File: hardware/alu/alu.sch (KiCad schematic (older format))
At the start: 68 parts, among them J1 Conn_ALU, J2 Conn_Power, U1 74LVC1G02, U10 74AUC2G04, U11 74HC4017, U12 74LVC1G157, U13 74HC595, U14 74HC86, U15 74LVC1G32, U16 74LVC1G08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

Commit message: Unified footprints
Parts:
- U21, U22, U23, U24, U5: footprint Package_TO_SOT_SMD:SOT-23-5 -> Package_TO_SOT_SMD:SOT-23-5_HandSoldering
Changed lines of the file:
@@
 F 0 "U5" H 14400 6617 50  0000 C CNN
 F 1 "MIC5504-3.3YM5" H 14400 6526 50  0000 C CNN
-F 2 "Package_TO_SOT_SMD:SOT-23-5" H 14400 5850 50  0001 C CNN
+F 2 "Package_TO_SOT_SMD:SOT-23-5_HandSoldering" H 14400 5850 50  0001 C CNN
 F 3 "http://ww1.microchip.com/downloads/en/DeviceDoc/MIC550X.pdf" H 14150 6500 50  0001 C CNN
 	1    14400 6250
@@
 F 0 "U21" H 19300 4017 50  0000 C CNN
 F 1 "74LVC1G04" H 19300 3926 50  0000 C CNN
-F 2 "Package_TO_SOT_SMD:SOT-23-5" H 19300 3750 50  0001 C CNN
+F 2 "Package_TO_SOT_SMD:SOT-23-5_HandSoldering" H 19300 3750 50  0001 C CNN
 F 3 "" H 19300 3750 50  0001 C CNN
 	1    19300 3750
@@
 F 0 "U21" H 19800 11150 50  0000 L CNN
 F 1 "74LVC1G04" V 19600 11550 50  0000 C CNN
-F 2 "Package_TO_SOT_SMD:SOT-23-5" H 19750 11550 50  0001 C CNN
+F 2 "Package_TO_SOT_SMD:SOT-23-5_HandSoldering" H 19750 11550 50  0001 C CNN
 F 3 "" H 19750 11550 50  0001 C CNN
 	2    19750 11550
@@
 F 0 "U23" H 19100 6217 50  0000 C CNN
 F 1 "74LVC1G04" H 19100 6126 50  0000 C CNN
-F 2 "Package_TO_SOT_SMD:SOT-23-5" H 19100 5950 50  0001 C CNN
+F 2 "Package_TO_SOT_SMD:SOT-23-5_HandSoldering" H 19100 5950 50  0001 C CNN
 F 3 "" H 19100 5950 50  0001 C CNN
 	1    19100 5950
@@
 F 0 "U22" H 21000 4017 50  0000 C CNN
 F 1 "74LVC1G04" H 21000 3926 50  0000 C CNN
-F 2 "Package_TO_SOT_SMD:SOT-23-5" H 21000 3750 50  0001 C CNN
+F 2 "Package_TO_SOT_SMD:SOT-23-5_HandSoldering" H 21000 3750 50  0001 C CNN
 F 3 "" H 21000 3750 50  0001 C CNN
 	1    21000 3750
@@
 F 0 "U24" H 20900 6267 50  0000 C CNN
 F 1 "74LVC1G04" H 20900 6176 50  0000 C CNN
-F 2 "Package_TO_SOT_SMD:SOT-23-5" H 20900 6000 50  0001 C CNN
+F 2 "Package_TO_SOT_SMD:SOT-23-5_HandSoldering" H 20900 6000 50  0001 C CNN
 F 3 "" H 20900 6000 50  0001 C CNN
 	1    20900 6000
@@
 F 0 "U22" H 20200 11150 50  0000 L CNN
 F 1 "74LVC1G04" V 20000 11550 50  0000 C CNN
-F 2 "Package_TO_SOT_SMD:SOT-23-5" H 20150 11550 50  0001 C CNN
+F 2 "Package_TO_SOT_SMD:SOT-23-5_HandSoldering" H 20150 11550 50  0001 C CNN
 F 3 "" H 20150 11550 50  0001 C CNN
 	2    20150 11550
@@
 F 0 "U23" H 20600 11150 50  0000 L CNN
 F 1 "74LVC1G04" V 20400 11550 50  0000 C CNN
-F 2 "Package_TO_SOT_SMD:SOT-23-5" H 20550 11550 50  0001 C CNN
+F 2 "Package_TO_SOT_SMD:SOT-23-5_HandSoldering" H 20550 11550 50  0001 C CNN
 F 3 "" H 20550 11550 50  0001 C CNN
 	2    20550 11550
@@
 F 0 "U24" H 21000 11150 50  0000 L CNN
 F 1 "74LVC1G04" V 20800 11550 50  0000 C CNN
-F 2 "Package_TO_SOT_SMD:SOT-23-5" H 20950 11550 50  0001 C CNN
+F 2 "Package_TO_SOT_SMD:SOT-23-5_HandSoldering" H 20950 11550 50  0001 C CNN
 F 3 "" H 20950 11550 50  0001 C CNN
 	2    20950 11550

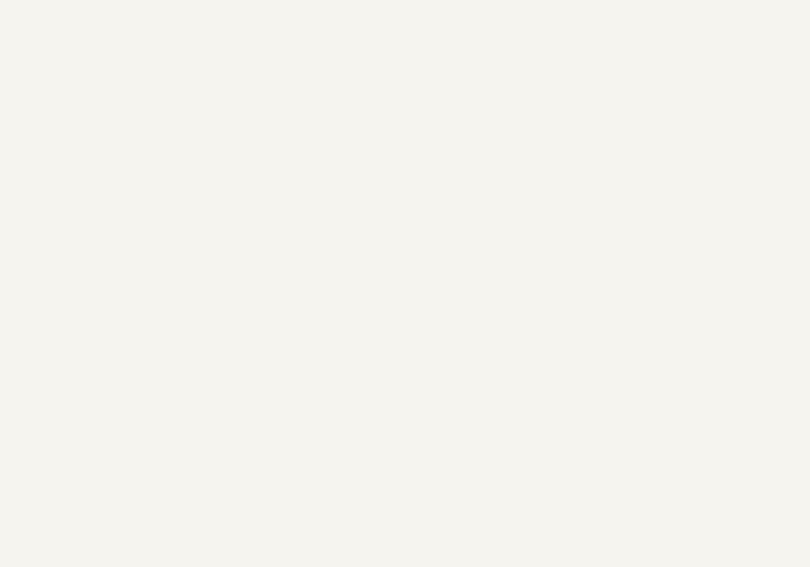
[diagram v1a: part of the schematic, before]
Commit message: Added test points
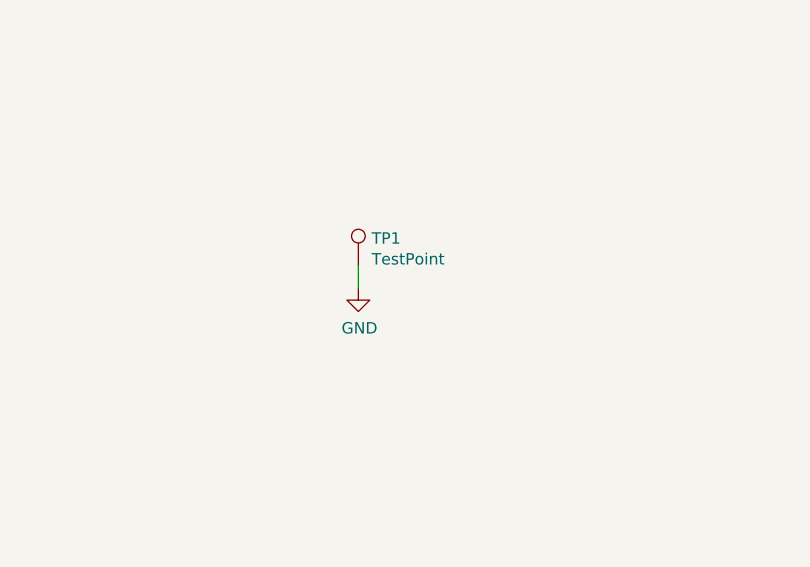
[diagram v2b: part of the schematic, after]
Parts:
- added TP1: TestPoint, TestPoint:TestPoint_THTPad_D2.0mm_Drill1.0mm, symbol Connector:TestPoint
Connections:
- net GND: now also TP1.1
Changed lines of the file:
@@
 	7950 1800 8500 1800
 $Comp
-L power:VCC #PWR02
+L power:VCC #PWR?
 U 1 1 5E136084
 P 11600 900
-F 0 "#PWR02" H 11600 750 50  0001 C CNN
+F 0 "#PWR?" H 11600 750 50  0001 C CNN
 F 1 "VCC" H 11617 1073 50  0000 C CNN
 F 2 "" H 11600 900 50  0001 C CNN
@@
 	11600 900  11600 1000
 $Comp
-L power:VCC #PWR03
+L power:VCC #PWR?
 U 1 1 5E136E49
 P 5550 1650
-F 0 "#PWR03" H 5550 1500 50  0001 C CNN
+F 0 "#PWR?" H 5550 1500 50  0001 C CNN
 F 1 "VCC" H 5567 1823 50  0000 C CNN
 F 2 "" H 5550 1650 50  0001 C CNN
@@
 	13950 1150 13200 1150
 $Comp
-L power:VCC #PWR01
+L power:VCC #PWR?
 U 1 1 5E278F9B
 P 14250 700
-F 0 "#PWR01" H 14250 550 50  0001 C CNN
+F 0 "#PWR?" H 14250 550 50  0001 C CNN
 F 1 "VCC" H 14267 873 50  0000 C CNN
 F 2 "" H 14250 700 50  0001 C CNN
@@
 P 8600 3400
 AR Path="/5E16DDE6/5EA50BD9" Ref="#PWR?"  Part="1"
-AR Path="/5EA50BD9" Ref="#PWR06"  Part="1"
-F 0 "#PWR06" H 8600 3250 50  0001 C CNN
+AR Path="/5EA50BD9" Ref="#PWR?"  Part="1"
+F 0 "#PWR?" H 8600 3250 50  0001 C CNN
 F 1 "VCC" H 8617 3573 50  0000 C CNN
 F 2 "" H 8600 3400 50  0001 C CNN
@@
 P 8600 5400
 AR Path="/5E16DDE6/5EA50BDF" Ref="#PWR?"  Part="1"
-AR Path="/5EA50BDF" Ref="#PWR013"  Part="1"
-F 0 "#PWR013" H 8600 5250 50  0001 C CNN
+AR Path="/5EA50BDF" Ref="#PWR?"  Part="1"
+F 0 "#PWR?" H 8600 5250 50  0001 C CNN
 F 1 "VCC" H 8617 5573 50  0000 C CNN
 F 2 "" H 8600 5400 50  0001 C CNN
@@
 P 8600 4900
 AR Path="/5E16DDE6/5EA50BE6" Ref="#PWR?"  Part="1"
-AR Path="/5EA50BE6" Ref="#PWR010"  Part="1"
-F 0 "#PWR010" H 8600 4650 50  0001 C CNN
+AR Path="/5EA50BE6" Ref="#PWR?"  Part="1"
+F 0 "#PWR?" H 8600 4650 50  0001 C CNN
 F 1 "GND" H 8605 4727 50  0000 C CNN
 F 2 "" H 8600 4900 50  0001 C CNN
@@
 P 8600 6900
 AR Path="/5E16DDE6/5EA50BF1" Ref="#PWR?"  Part="1"
-AR Path="/5EA50BF1" Ref="#PWR015"  Part="1"
-F 0 "#PWR015" H 8600 6650 50  0001 C CNN
+AR Path="/5EA50BF1" Ref="#PWR?"  Part="1"
+F 0 "#PWR?" H 8600 6650 50  0001 C CNN
 F 1 "GND" H 8605 6727 50  0000 C CNN
 F 2 "" H 8600 6900 50  0001 C CNN
@@
 P 9900 5150
 AR Path="/5E16DDE6/5EA50BF8" Ref="#PWR?"  Part="1"
-AR Path="/5EA50BF8" Ref="#PWR012"  Part="1"
-F 0 "#PWR012" H 9900 4900 50  0001 C CNN
+AR Path="/5EA50BF8" Ref="#PWR?"  Part="1"
+F 0 "#PWR?" H 9900 4900 50  0001 C CNN
 F 1 "GND" H 9905 4977 50  0000 C CNN
 F 2 "" H 9900 5150 50  0001 C CNN
@@
 P 10000 3450
 AR Path="/5E16DDE6/5EA50C02" Ref="#PWR?"  Part="1"
-AR Path="/5EA50C02" Ref="#PWR07"  Part="1"
-F 0 "#PWR07" H 10000 3300 50  0001 C CNN
+AR Path="/5EA50C02" Ref="#PWR?"  Part="1"
+F 0 "#PWR?" H 10000 3300 50  0001 C CNN
 F 1 "VCC" H 10017 3623 50  0000 C CNN
 F 2 "" H 10000 3450 50  0001 C CNN
@@
 P 2850 4800
 AR Path="/5E16DDE6/5ECDCE5A" Ref="#PWR?"  Part="1"
-AR Path="/5ECDCE5A" Ref="#PWR09"  Part="1"
-F 0 "#PWR09" H 2850 4650 50  0001 C CNN
+AR Path="/5ECDCE5A" Ref="#PWR?"  Part="1"
+F 0 "#PWR?" H 2850 4650 50  0001 C CNN
 F 1 "VCC" H 2867 4973 50  0000 C CNN
 F 2 "" H 2850 4800 50  0001 C CNN
@@
 P 2850 6700
 AR Path="/5E16DDE6/5ECEB98B" Ref="#PWR?"  Part="1"
-AR Path="/5ECEB98B" Ref="#PWR014"  Part="1"
-F 0 "#PWR014" H 2850 6450 50  0001 C CNN
+AR Path="/5ECEB98B" Ref="#PWR?"  Part="1"
+F 0 "#PWR?" H 2850 6450 50  0001 C CNN
 F 1 "GND" H 2855 6527 50  0000 C CNN
 F 2 "" H 2850 6700 50  0001 C CNN
@@
 $EndComp
 $Comp
-L power:GND #PWR011
+L power:GND #PWR?
 U 1 1 5F2733B8
 P 14500 5050
-F 0 "#PWR011" H 14500 4800 50  0001 C CNN
+F 0 "#PWR?" H 14500 4800 50  0001 C CNN
 F 1 "GND" H 14505 4877 50  0000 C CNN
 F 2 "" H 14500 5050 50  0001 C CNN
@@
 P 14500 2850
 AR Path="/5E16DDE6/5F2EB63E" Ref="#PWR?"  Part="1"
-AR Path="/5F2EB63E" Ref="#PWR05"  Part="1"
-F 0 "#PWR05" H 14500 2700 50  0001 C CNN
+AR Path="/5F2EB63E" Ref="#PWR?"  Part="1"
+F 0 "#PWR?" H 14500 2700 50  0001 C CNN
 F 1 "VCC" H 14517 3023 50  0000 C CNN
 F 2 "" H 14500 2850 50  0001 C CNN
@@
 P 1900 3750
 AR Path="/5E16DDE6/5F44E000" Ref="#PWR?"  Part="1"
-AR Path="/5F44E000" Ref="#PWR08"  Part="1"
-F 0 "#PWR08" H 1900 3500 50  0001 C CNN
+AR Path="/5F44E000" Ref="#PWR?"  Part="1"
+F 0 "#PWR?" H 1900 3500 50  0001 C CNN
 F 1 "GND" H 1905 3577 50  0000 C CNN
 F 2 "" H 1900 3750 50  0001 C CNN
@@
 	14900 2300 15150 2300
 $Comp
-L power:PWR_FLAG #FLG01
+L power:PWR_FLAG #FLG?
 U 1 1 5F7D3DC4
 P 13450 6050
-F 0 "#FLG01" H 13450 6125 50  0001 C CNN
+F 0 "#FLG?" H 13450 6125 50  0001 C CNN
 F 1 "PWR_FLAG" H 13450 6224 50  0000 C CNN
 F 2 "" H 13450 6050 50  0001 C CNN
@@
 P 14950 10900
 AR Path="/5E16DDE6/5F9966CD" Ref="#PWR?"  Part="1"
-AR Path="/5F9966CD" Ref="#PWR0101"  Part="1"
-F 0 "#PWR0101" H 14950 10750 50  0001 C CNN
+AR Path="/5F9966CD" Ref="#PWR?"  Part="1"
+F 0 "#PWR?" H 14950 10750 50  0001 C CNN
 F 1 "VCC" H 14967 11073 50  0000 C CNN
 F 2 "" H 14950 10900 50  0001 C CNN
@@
 	15350 11000 15750 11000
 $Comp
-L power:PWR_FLAG #FLG02
+L power:PWR_FLAG #FLG?
 U 1 1 5FC151D8
 P 13450 6750
-F 0 "#FLG02" H 13450 6825 50  0001 C CNN
+F 0 "#FLG?" H 13450 6825 50  0001 C CNN
 F 1 "PWR_FLAG" H 13450 6923 50  0000 C CNN
 F 2 "" H 13450 6750 50  0001 C CNN
@@
 P 13000 12800
 AR Path="/5E16DDE6/5FCB6F4E" Ref="#PWR?"  Part="1"
-AR Path="/5FCB6F4E" Ref="#PWR016"  Part="1"
-F 0 "#PWR016" H 13000 12650 50  0001 C CNN
+AR Path="/5FCB6F4E" Ref="#PWR?"  Part="1"
+F 0 "#PWR?" H 13000 12650 50  0001 C CNN
 F 1 "VCC" H 13017 12973 50  0000 C CNN
 F 2 "" H 13000 12800 50  0001 C CNN
@@
 P 13000 13300
 AR Path="/5E16DDE6/5FCEDEFB" Ref="#PWR?"  Part="1"
-AR Path="/5FCEDEFB" Ref="#PWR017"  Part="1"
-F 0 "#PWR017" H 13000 13050 50  0001 C CNN
+AR Path="/5FCEDEFB" Ref="#PWR?"  Part="1"
+F 0 "#PWR?" H 13000 13050 50  0001 C CNN
 F 1 "GND" H 13005 13127 50  0000 C CNN
 F 2 "" H 13000 13300 50  0001 C CNN
@@
 P 12900 6750
 AR Path="/5E16DDE6/5EE78A02" Ref="#PWR?"  Part="1"
-AR Path="/5EE78A02" Ref="#PWR0102"  Part="1"
-F 0 "#PWR0102" H 12900 6500 50  0001 C CNN
+AR Path="/5EE78A02" Ref="#PWR?"  Part="1"
+F 0 "#PWR?" H 12900 6500 50  0001 C CNN
 F 1 "GND" H 12905 6577 50  0000 C CNN
 F 2 "" H 12900 6750 50  0001 C CNN
@@
 P 15300 6050
 AR Path="/5E16DDE6/5EEBF755" Ref="#PWR?"  Part="1"
-AR Path="/5EEBF755" Ref="#PWR0103"  Part="1"
-F 0 "#PWR0103" H 15300 5900 50  0001 C CNN
+AR Path="/5EEBF755" Ref="#PWR?"  Part="1"
+F 0 "#PWR?" H 15300 5900 50  0001 C CNN
 F 1 "VCC" H 15317 6223 50  0000 C CNN
 F 2 "" H 15300 6050 50  0001 C CNN
@@
 P 15300 6750
 AR Path="/5E16DDE6/5EF0698B" Ref="#PWR?"  Part="1"
-AR Path="/5EF0698B" Ref="#PWR0104"  Part="1"
-F 0 "#PWR0104" H 15300 6500 50  0001 C CNN
+AR Path="/5EF0698B" Ref="#PWR?"  Part="1"
+F 0 "#PWR?" H 15300 6500 50  0001 C CNN
 F 1 "GND" H 15305 6577 50  0000 C CNN
 F 2 "" H 15300 6750 50  0001 C CNN
@@
 P 14950 12200
 AR Path="/5E16DDE6/5F04A9E1" Ref="#PWR?"  Part="1"
-AR Path="/5F04A9E1" Ref="#PWR0105"  Part="1"
-F 0 "#PWR0105" H 14950 11950 50  0001 C CNN
+AR Path="/5F04A9E1" Ref="#PWR?"  Part="1"
+F 0 "#PWR?" H 14950 11950 50  0001 C CNN
 F 1 "GND" H 14955 12027 50  0000 C CNN
 F 2 "" H 14950 12200 50  0001 C CNN
@@
 P 19800 2600
 AR Path="/5E16DDE6/5F7FA302" Ref="#PWR?"  Part="1"
-AR Path="/5F7FA302" Ref="#PWR04"  Part="1"
-F 0 "#PWR04" H 19800 2450 50  0001 C CNN
+AR Path="/5F7FA302" Ref="#PWR?"  Part="1"
+F 0 "#PWR?" H 19800 2450 50  0001 C CNN
 F 1 "VCC" H 19817 2773 50  0000 C CNN
 F 2 "" H 19800 2600 50  0001 C CNN
@@
 P 21700 2600
 AR Path="/5E16DDE6/5F9B3A0A" Ref="#PWR?"  Part="1"
-AR Path="/5F9B3A0A" Ref="#PWR018"  Part="1"
-F 0 "#PWR018" H 21700 2450 50  0001 C CNN
+AR Path="/5F9B3A0A" Ref="#PWR?"  Part="1"
+F 0 "#PWR?" H 21700 2450 50  0001 C CNN
 F 1 "VCC" H 21717 2773 50  0000 C CNN
 F 2 "" H 21700 2600 50  0001 C CNN
@@
 P 19800 4800
 AR Path="/5E16DDE6/5F9DCD90" Ref="#PWR?"  Part="1"
-AR Path="/5F9DCD90" Ref="#PWR021"  Part="1"
-F 0 "#PWR021" H 19800 4650 50  0001 C CNN
+AR Path="/5F9DCD90" Ref="#PWR?"  Part="1"
+F 0 "#PWR?" H 19800 4650 50  0001 C CNN
 F 1 "VCC" H 19817 4973 50  0000 C CNN
 F 2 "" H 19800 4800 50  0001 C CNN
@@
 P 21750 4800
 AR Path="/5E16DDE6/5FA08230" Ref="#PWR?"  Part="1"
-AR Path="/5FA08230" Ref="#PWR022"  Part="1"
-F 0 "#PWR022" H 21750 4650 50  0001 C CNN
+AR Path="/5FA08230" Ref="#PWR?"  Part="1"
+F 0 "#PWR?" H 21750 4650 50  0001 C CNN
 F 1 "VCC" H 21767 4973 50  0000 C CNN
 F 2 "" H 21750 4800 50  0001 C CNN
@@
 	1    0    0    1
 $EndComp
+$Comp
+L Connector:TestPoint TP1
+U 1 1 5EF26A44
+P 12250 8800
+F 0 "TP1" H 12308 8920 50  0000 L CNN
+F 1 "TestPoint" H 12308 8829 50  0000 L CNN
+F 2 "TestPoint:TestPoint_THTPad_D2.0mm_Drill1.0mm" H 12450 8800 50  0001 C CNN
+F 3 "~" H 12450 8800 50  0001 C CNN
+	1    12250 8800
+	1    0    0    -1
+$EndComp
+$Comp
+L power:GND #PWR?
+U 1 1 5EF26B64
+P 12250 8900
+AR Path="/5E16DDE6/5EF26B64" Ref="#PWR?"  Part="1"
+AR Path="/5EF26B64" Ref="#PWR?"  Part="1"
+F 0 "#PWR?" H 12250 8650 50  0001 C CNN
+F 1 "GND" H 12255 8727 50  0000 C CNN
+F 2 "" H 12250 8900 50  0001 C CNN
+F 3 "" H 12250 8900 50  0001 C CNN
+	1    12250 8900
+	1    0    0    -1
+$EndComp
+Wire Wire Line
+	12250 8800 12250 8900
 $EndSCHEMATC
